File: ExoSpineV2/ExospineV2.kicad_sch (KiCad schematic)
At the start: 36 parts, among them J1 GPIO, J15 Conn_01x02, J16 Conn_01x02, J17 Conn_01x02, J18 Screw_Terminal_01x01, J19 Conn_01x03, J20 Conn_01x03, J24 Conn_01x02, J25 Conn_01x03, J26 Conn_01x03, J27 Conn_01x04, J28 Conn_01x03, J29 Conn_01x03, Q6 Q_NMOS_DGS, Q7 Q_NMOS_DGS, Q8 Q_NMOS_DGS, U6 MCP3008

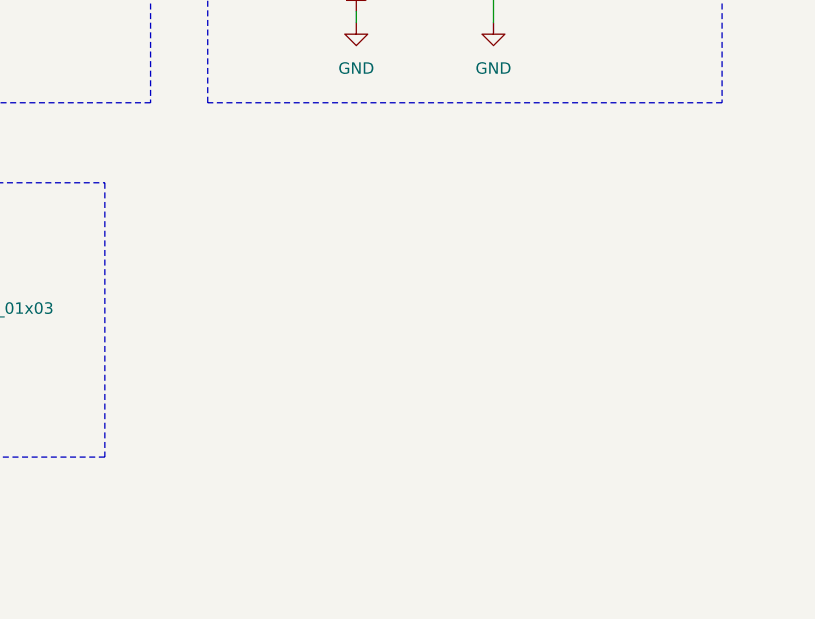
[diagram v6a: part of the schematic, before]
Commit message: Added Pressure Sensor Backup
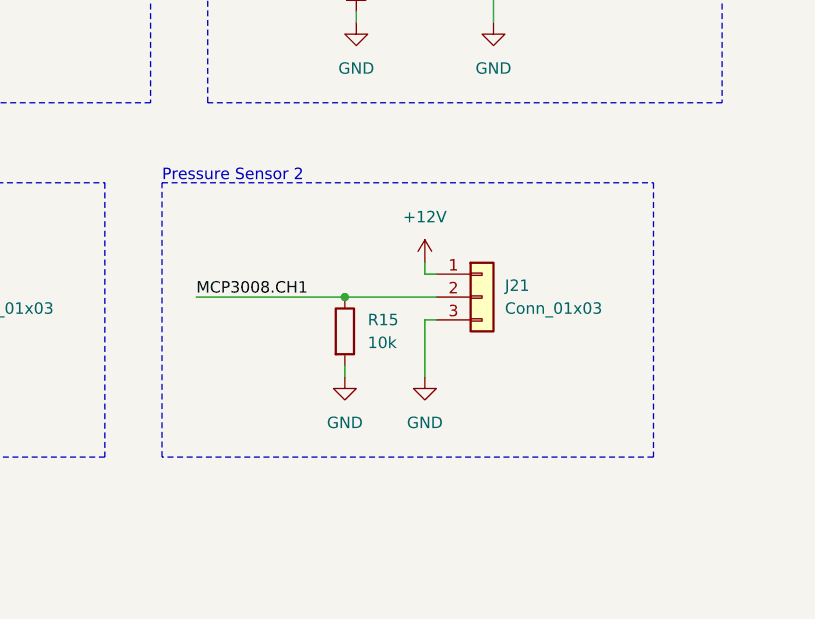
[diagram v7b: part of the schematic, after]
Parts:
- added J21: Conn_01x03, symbol Connector_Generic:Conn_01x03
- added R15: 10k, symbol Device:R
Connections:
- net +12V: now also J21.1 (Pin_1)
- net GND: now also J21.3 (Pin_3), R15.2
- net MCP3008.CH1: now also J21.2 (Pin_2), R15.1
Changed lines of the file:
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@@
   (junction (at 76.2 27.94) (diameter 1.016) (color 0 0 0 0)
+  )
+  (junction (at 351.79 116.84) (diameter 0) (color 0 0 0 0)
   )
   (junction (at 111.76 146.05) (diameter 0) (color 0 0 0 0)
@@
     (stroke (width 0) (type default))
   )
+  (wire (pts (xy 360.68 114.3) (xy 360.68 113.03))
+    (stroke (width 0) (type default))
+  )
   (wire (pts (xy 119.38 148.59) (xy 119.38 166.37))
     (stroke (width 0) (type default))
@@
     (stroke (width 0) (type default))
   )
+  (wire (pts (xy 351.79 125.73) (xy 351.79 124.46))
+    (stroke (width 0) (type default))
+  )
   (wire (pts (xy 100.33 148.59) (xy 119.38 148.59))
     (stroke (width 0) (type default))
@@
     (stroke (width 0) (type default))
   )
+  (wire (pts (xy 360.68 114.3) (xy 361.95 114.3))
+    (stroke (width 0) (type default))
+  )
   (wire (pts (xy 223.52 165.1) (xy 223.52 163.83))
     (stroke (width 0) (type default))
@@
     (stroke (width 0) (type default))
   )
+  (wire (pts (xy 351.79 116.84) (xy 361.95 116.84))
+    (stroke (width 0) (type default))
+  )
   (wire (pts (xy 76.2 27.94) (xy 76.2 30.48))
     (stroke (width 0) (type solid))
@@
     (stroke (width 0) (type default))
   )
+  (wire (pts (xy 360.68 125.73) (xy 360.68 119.38))
+    (stroke (width 0) (type default))
+  )
   (wire (pts (xy 100.33 151.13) (xy 127 151.13))
     (stroke (width 0) (type default))
@@
     (stroke (width 0) (type default))
   )
+  (wire (pts (xy 335.28 116.84) (xy 351.79 116.84))
+    (stroke (width 0) (type default))
+  )
   (wire (pts (xy 76.2 63.5) (xy 73.66 63.5))
     (stroke (width 0) (type solid))
@@
   )
   (wire (pts (xy 59.69 151.13) (xy 59.69 158.75))
+    (stroke (width 0) (type default))
+  )
+  (wire (pts (xy 360.68 119.38) (xy 361.95 119.38))
     (stroke (width 0) (type default))
   )
@@
     (fill (type none))
   )
+  (rectangle (start 331.47 104.14) (end 386.08 134.62)
+    (stroke (width 0) (type dash) (color 194 0 0 1))
+    (fill (type none))
+  )
   (rectangle (start 19.05 124.46) (end 187.96 182.88)
     (stroke (width 0) (type dash) (color 0 194 0 1))
@@
     (effects (font (size 1.27 1.27) (color 132 132 132 1)) (justify left bottom))
   )
+  (text "Pressure Sensor 2" (at 331.47 104.14 0)
+    (effects (font (size 1.27 1.27) (color 194 0 0 1)) (justify left bottom))
+  )
   (text "GPS" (at 260.35 20.32 0)
     (effects (font (size 1.27 1.27)) (justify left bottom))
@@
   (label "MCP3008.CH0" (at 177.8 143.51 180) (fields_autoplaced)
     (effects (font (size 1.27 1.27)) (justify right bottom))
+  )
+  (label "MCP3008.CH1" (at 335.28 116.84 0) (fields_autoplaced)
+    (effects (font (size 1.27 1.27)) (justify left bottom))
   )
   (label "ID_SCL" (at 100.33 60.96 180) (fields_autoplaced)
@@
     )
   )
+  (symbol (lib_id "Device:R") (at 351.79 120.65 0) (unit 1)
+    (in_bom yes) (on_board yes) (dnp no) (fields_autoplaced)
+    (property "Reference" "R15" (at 354.33 119.38 0)
+      (effects (font (size 1.27 1.27)) (justify left))
+    )
+    (property "Value" "10k" (at 354.33 121.92 0)
+      (effects (font (size 1.27 1.27)) (justify left))
+    )
+    (property "Footprint" "" (at 350.012 120.65 90)
+      (effects (font (size 1.27 1.27)) hide)
+    )
+    (property "Datasheet" "~" (at 351.79 120.65 0)
+      (effects (font (size 1.27 1.27)) hide)
+    )
+    (pin "1")
+    (pin "2")
+    (instances
+      (project "ExospineV2"
+        (path "/e63e39d7-6ac0-4ffd-8aa3-1841a4541b55"
+          (reference "R15") (unit 1)
+        )
+      )
+    )
+  )
   (symbol (lib_id "Device:R") (at 289.56 81.28 0) (unit 1)
     (in_bom yes) (on_board yes) (dnp no) (fields_autoplaced)
@@
         (path "/e63e39d7-6ac0-4ffd-8aa3-1841a4541b55"
           (reference "J26") (unit 1)
+        )
+      )
+    )
+  )
+  (symbol (lib_id "Connector_Generic:Conn_01x03") (at 367.03 116.84 0) (unit 1)
+    (in_bom yes) (on_board yes) (dnp no) (fields_autoplaced)
+    (property "Reference" "J21" (at 369.57 115.57 0)
+      (effects (font (size 1.27 1.27)) (justify left))
+    )
+    (property "Value" "Conn_01x03" (at 369.57 118.11 0)
+      (effects (font (size 1.27 1.27)) (justify left))
+    )
+    (property "Footprint" "" (at 367.03 116.84 0)
+      (effects (font (size 1.27 1.27)) hide)
+    )
+    (property "Datasheet" "~" (at 367.03 116.84 0)
+      (effects (font (size 1.27 1.27)) hide)
+    )
+    (pin "3")
+    (pin "2")
+    (pin "1")
+    (instances
+      (project "ExospineV2"
+        (path "/e63e39d7-6ac0-4ffd-8aa3-1841a4541b55"
+          (reference "J21") (unit 1)
         )
       )
@@
     )
   )
+  (symbol (lib_id "power:+12V") (at 360.68 113.03 0) (unit 1)
+    (in_bom yes) (on_board yes) (dnp no) (fields_autoplaced)
+    (property "Reference" "#PWR039" (at 360.68 116.84 0)
+      (effects (font (size 1.27 1.27)) hide)
+    )
+    (property "Value" "+12V" (at 360.68 107.95 0)
+      (effects (font (size 1.27 1.27)))
+    )
+    (property "Footprint" "" (at 360.68 113.03 0)
+      (effects (font (size 1.27 1.27)) hide)
+    )
+    (property "Datasheet" "" (at 360.68 113.03 0)
+      (effects (font (size 1.27 1.27)) hide)
+    )
+    (pin "1")
+    (instances
+      (project "ExospineV2"
+        (path "/e63e39d7-6ac0-4ffd-8aa3-1841a4541b55"
+          (reference "#PWR039") (unit 1)
+        )
+      )
+    )
+  )
   (symbol (lib_name "GND_1") (lib_id "power:GND") (at 241.3 86.36 0) (unit 1)
     (in_bom yes) (on_board yes) (dnp no) (fields_autoplaced)
@@
         (path "/e63e39d7-6ac0-4ffd-8aa3-1841a4541b55"
           (reference "C33") (unit 1)
+        )
+      )
+    )
+  )
+  (symbol (lib_name "GND_2") (lib_id "power:GND") (at 351.79 125.73 0) (unit 1)
+    (in_bom yes) (on_board yes) (dnp no) (fields_autoplaced)
+    (property "Reference" "#PWR038" (at 351.79 132.08 0)
+      (effects (font (size 1.27 1.27)) hide)
+    )
+    (property "Value" "GND" (at 351.79 130.81 0)
+      (effects (font (size 1.27 1.27)))
+    )
+    (property "Footprint" "" (at 351.79 125.73 0)
+      (effects (font (size 1.27 1.27)) hide)
+    )
+    (property "Datasheet" "" (at 351.79 125.73 0)
+      (effects (font (size 1.27 1.27)) hide)
+    )
+    (pin "1")
+    (instances
+      (project "ExospineV2"
+        (path "/e63e39d7-6ac0-4ffd-8aa3-1841a4541b55"
+          (reference "#PWR038") (unit 1)
         )
       )
@@
         )
       )
+    )
+  )
+  (symbol (lib_name "GND_2") (lib_id "power:GND") (at 360.68 125.73 0) (unit 1)
+    (in_bom yes) (on_board yes) (dnp no) (fields_autoplaced)
+    (property "Reference" "#PWR040" (at 360.68 132.08 0)
+      (effects (font (size 1.27 1.27)) hide)
+    )
+    (property "Value" "GND" (at 360.68 130.81 0)
+      (effects (font (size 1.27 1.27)))
+    )
+    (property "Footprint" "" (at 360.68 125.73 0)
+      (effects (font (size 1.27 1.27)) hide)
+    )
+    (property "Datasheet" "" (at 360.68 125.73 0)
+      (effects (font (size 1.27 1.27)) hide)
+    )
+    (pin "1")
+    (instances
+      (project "ExospineV2"
+        (path "/e63e39d7-6ac0-4ffd-8aa3-1841a4541b55"
+          (reference "#PWR040") (unit 1)
+        )
+      )

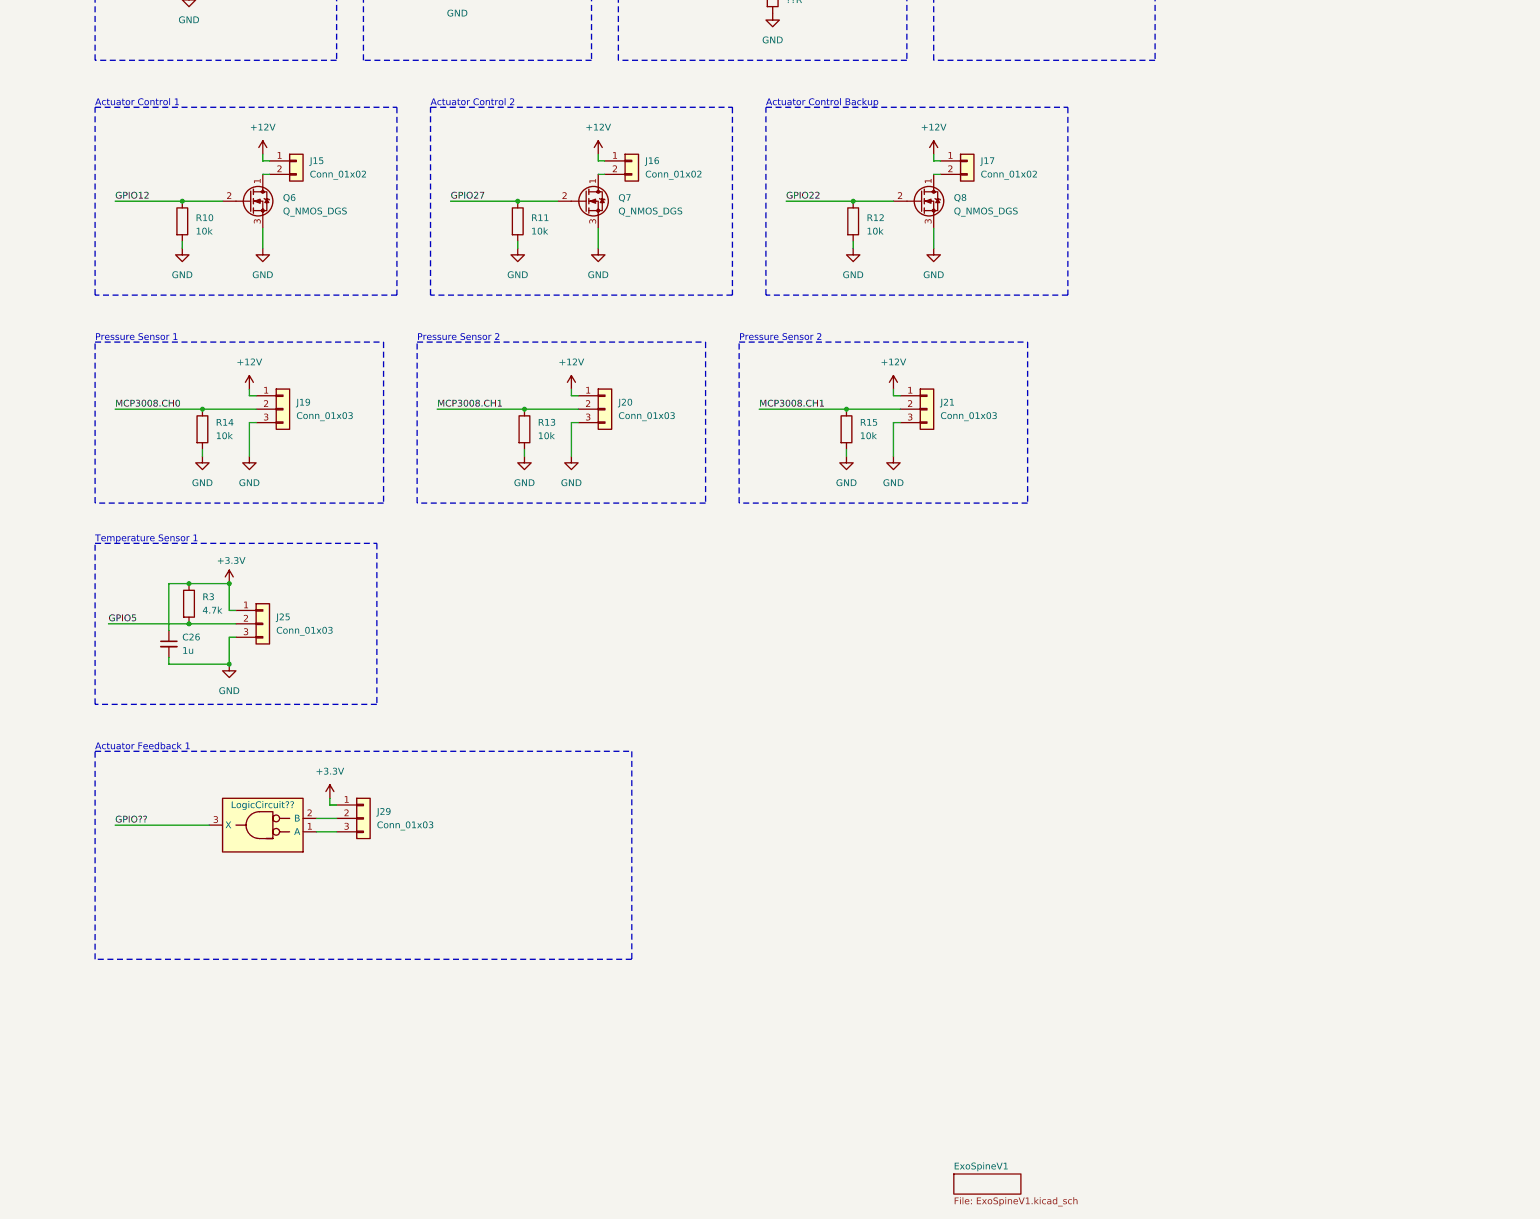
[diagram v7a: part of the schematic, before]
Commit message: Correction for Actuator Controls (12V down to 5V)
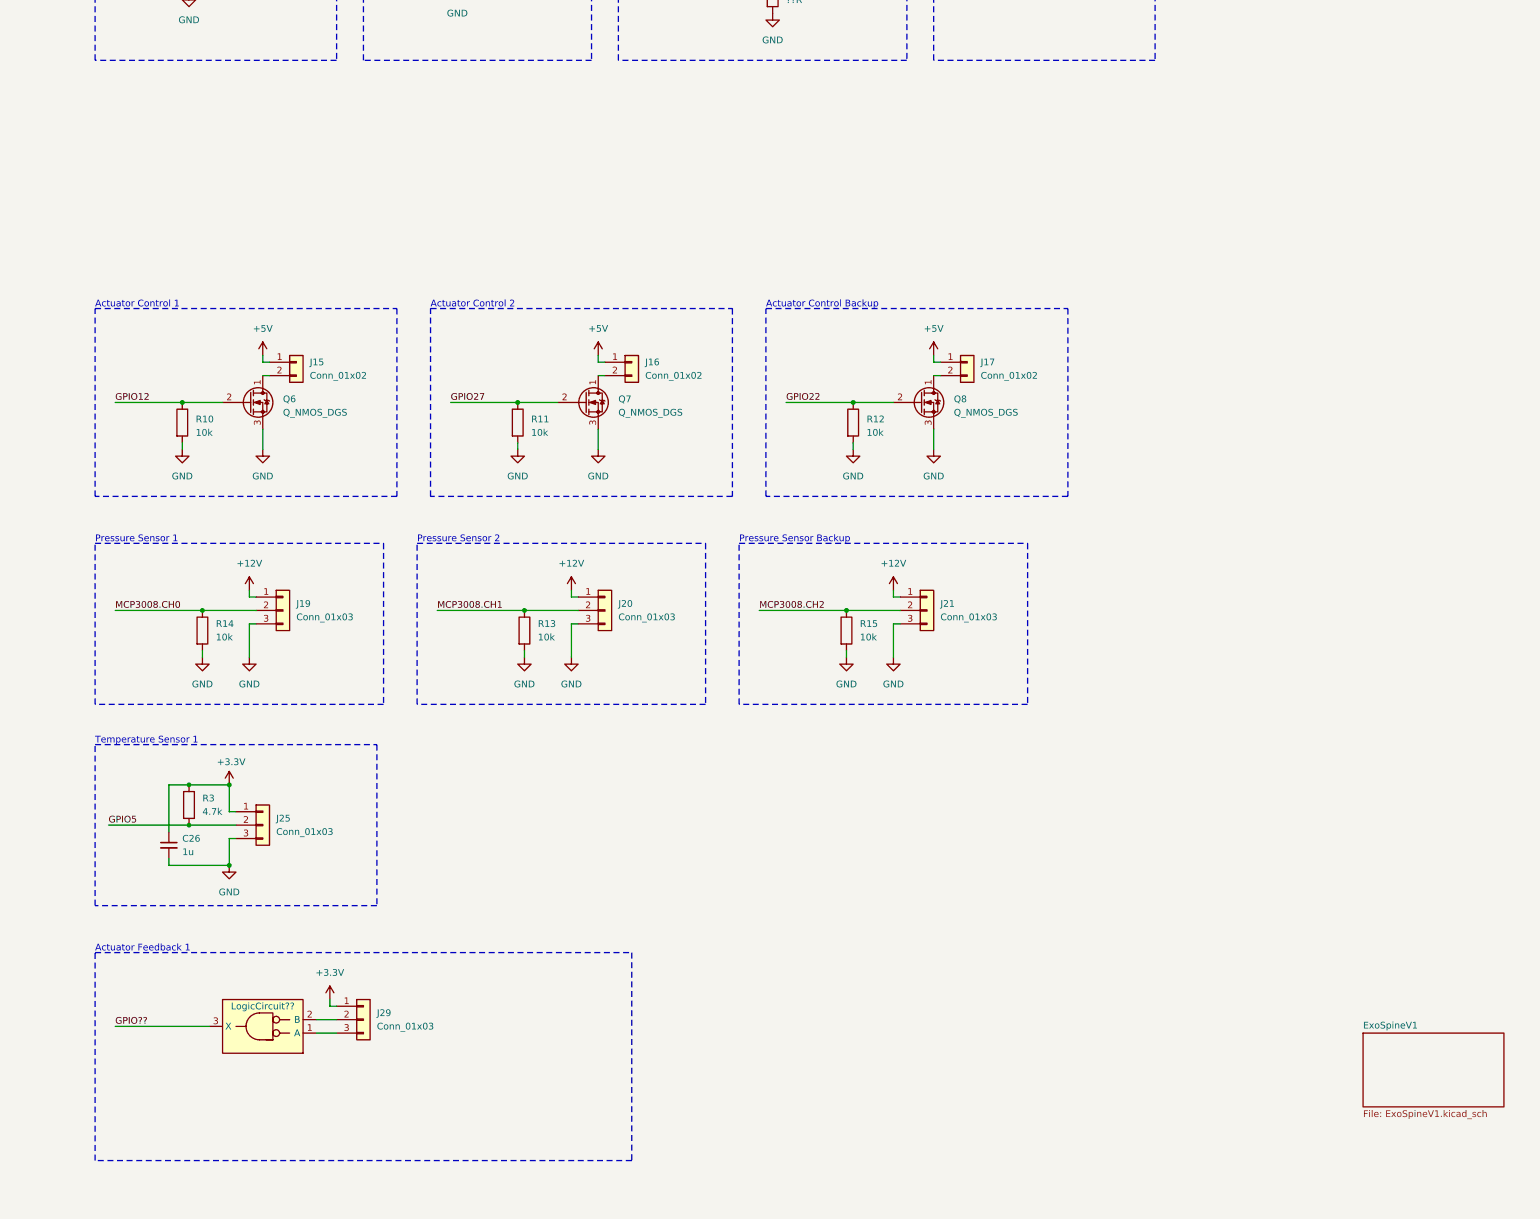
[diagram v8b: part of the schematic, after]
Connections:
- net +12V: no longer J15.1 (Pin_1), J16.1 (Pin_1), J17.1 (Pin_1)
- net +5V: now also J15.1 (Pin_1), J16.1 (Pin_1), J17.1 (Pin_1)
- net MCP3008.CH1: no longer J21.2 (Pin_2), R15.1
- net MCP3008.CH2: now also J21.2 (Pin_2), R15.1
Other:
- note added: "Pressure Sensor Backup"
- moved on the sheet: C26, J15, J16, J17, J19, J20, J21, J25, J29, LogicCircuit??, Q6, Q7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
